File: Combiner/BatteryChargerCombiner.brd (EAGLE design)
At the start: 190.5 x 40.6 mm, 201 parts, among them Q1 DMN6040SSD-13, Q10 4.3A/20V/54mΩ, Q11 4.3A/20V/54mΩ, Q2 DMN6040SSD-13, Q3 DMN6040SSD-13, Q4 DMN6040SSD-13, Q5 DMP4047SSD-13, Q6 220mA/50V/3.5Ω, Q7 220mA/50V/3.5Ω, Q8 4.3A/20V/54mΩ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

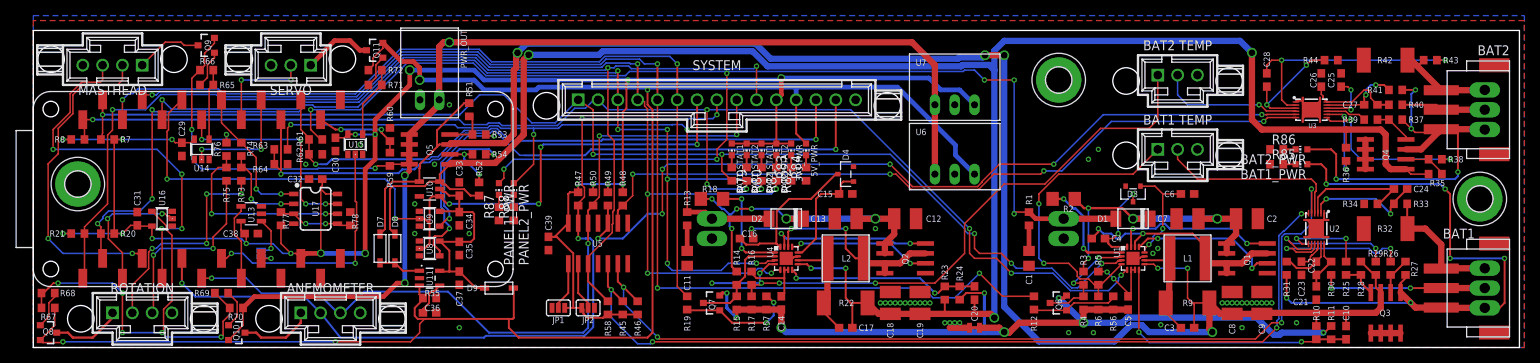
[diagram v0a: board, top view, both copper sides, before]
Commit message: Put together BoM for battery charger/combiner. Left out everything except the trim resistors for the temp sensor'
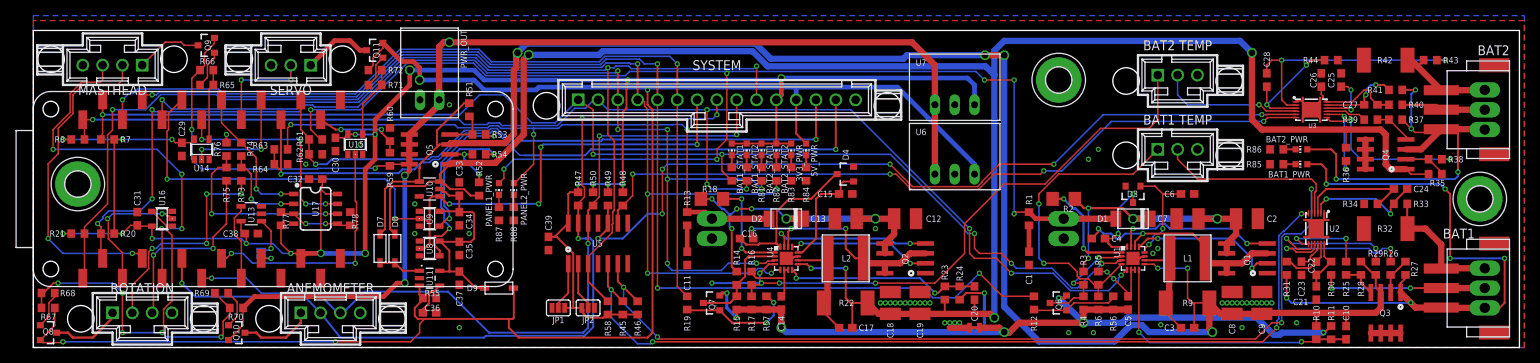
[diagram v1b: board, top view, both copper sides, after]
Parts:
- C1, C11: device resistor:C0805 -> resistor:C0603
- D3, D4: value (none) -> 700mA/40V/533mV; device adafruit:SOT23-R -> SparkFun-DiscreteSemi:SOT23-3
- R10, R23: value (none) -> 300K
- R11, R24: value (none) -> 100K
- R14, R3: value (none) -> 232K
- R15, R4, R59, R74, R76: value (none) -> 15K
- R20, R21, R60, R7, R73, R75, R77, R78, R8: value (none) -> 10K
- R22, R9: value 20m -> 40m
- R32, R42: value (none) -> 2m
- R61, R63: value (none) -> 75K
- R62, R64: value (none) -> 12K
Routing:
- net +3V3: track 269.5 -> 271.0 mm
